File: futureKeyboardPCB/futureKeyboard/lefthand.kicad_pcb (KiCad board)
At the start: 2 copper layers, 168.9 x 88.3 mm, 126 parts, among them J1 Conn_01x01, J10 Conn_01x02, J11 Conn_01x01, J12 Conn_01x01, J13 Conn_01x04, J14 Conn_01x06, J15 Conn_01x06, J16 Conn_01x01, J17 Conn_01x15, J18 Conn_01x15, J19 Conn_01x15, J2 Conn_01x02, J20 Conn_01x15, J21 Conn_01x04, J22 Conn_01x04, J23 Conn_01x04, J24 Conn_01x04, J25 Conn_01x02, J26 Conn_01x01, J27 Conn_01x01, J28 Conn_01x01, J29 Conn_01x01, J3 Conn_01x01, J30 Conn_01x01, J31 Conn_01x01, J32 Conn_01x01, J33 Conn_01x01, J4 Conn_01x01, J5 Conn_01x04, J6 Conn_01x06, J7 Conn_01x06, J8 Conn_01x01, J9 Conn_01x01, P1 CONN_01X02, P2 CONN_01X06, P3 CONN_01X02, P4 CONN_01X06, Q1 2SC1815, Q2 2SC1815, Q3 2SC1815, Q4 2SC1815, Q5 2SC1815, Q6 2SC1815, SW1 SW_SPDT, SW10 SW_Push, SW11 SW_Push, SW12 SW_Push, SW13 SW_Push, SW14 SW_Push, SW15 SW_Push, SW16 SW_Push, SW17 SW_Push, SW18 SW_Push, SW19 SW_Push, SW2 SW_Push, SW20 SW_Push, SW21 SW_Push, SW22 SW_Push, SW23 SW_Push, SW24 SW_Push, SW25 SW_Push, SW3 SW_Push, SW4 SW_Push, SW5 SW_Push, SW6 SW_Push, SW7 SW_Push, SW8 SW_Push, SW9 SW_SPDT, U1 AMS1117-1.5, U2 ESP32, U3 AMS1117-1.5, U4 ESP32, U5 joystick

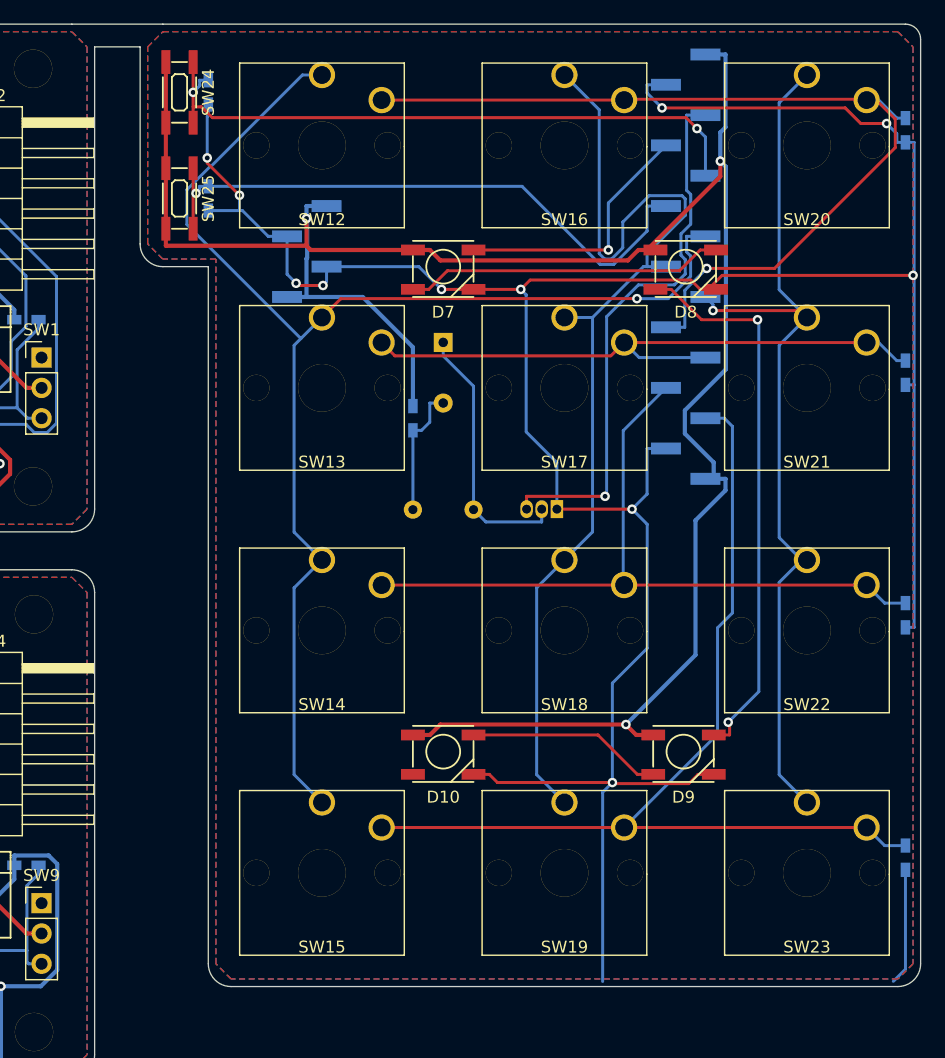
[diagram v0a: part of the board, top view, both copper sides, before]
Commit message: add arduino project using esp-now, new PCB
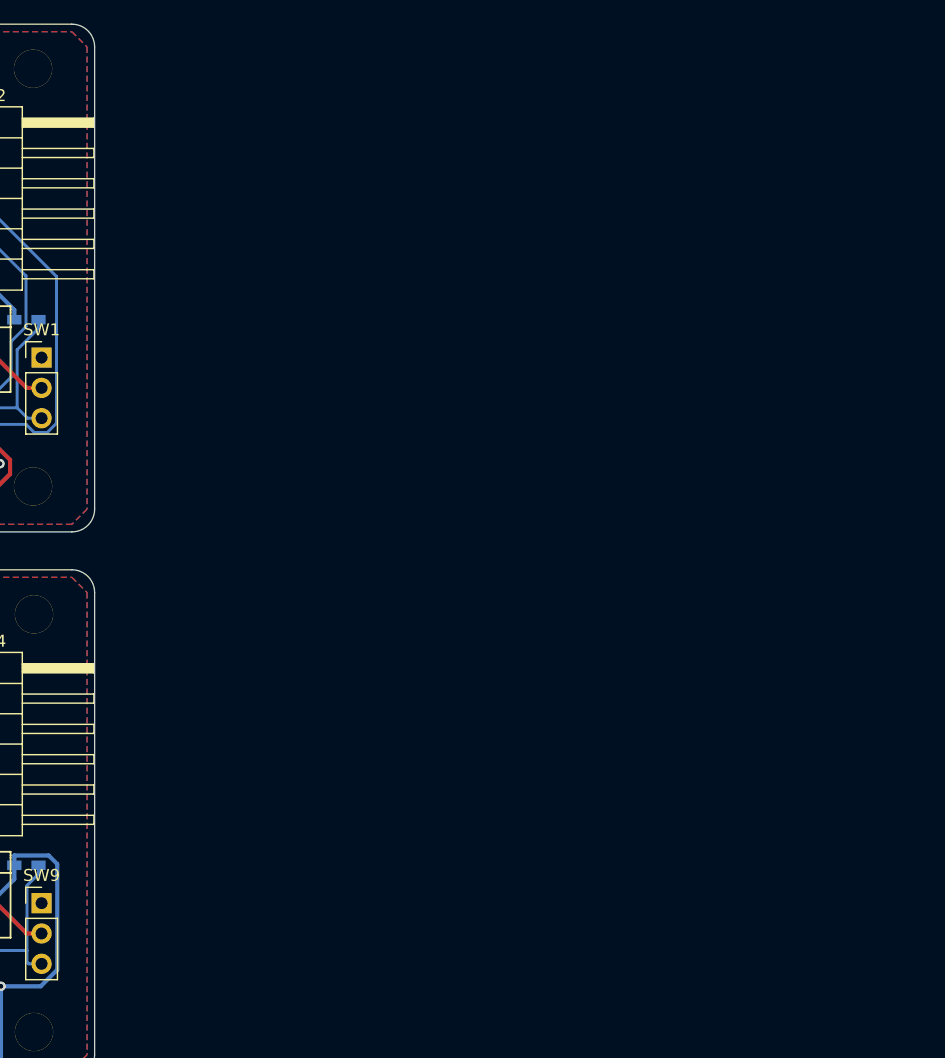
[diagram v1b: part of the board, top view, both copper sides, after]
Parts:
- removed D10, D7, D8, D9: WS2812B, akizukit:WS2812B
- removed D6: DIODE, Diode_THT:D_DO-35_SOD27_P5.08mm_Vertical_KathodeUp
- removed J20: Conn_01x15, Connector_PinHeader_2.54mm:PinHeader_1x15_P2.54mm_Vertical_SMD_Pin1Left
- removed J24: Conn_01x04, Connector_PinHeader_2.54mm:PinHeader_1x04_P2.54mm_Vertical_SMD_Pin1Left
- removed LS2: Speaker, akizukit:small_speaker
- removed Q6: 2SC1815, Package_TO_SOT_THT:TO-92_Inline
- removed R18, R20, R21, R22, R23, R24, R25: 1k, akizukit:SMD-1608
- removed SW12, SW13, SW14, SW15, SW16, SW17, SW18, SW19, SW20, SW21, SW22, SW23: SW_Push, akizukit:keySwitch
- removed SW24, SW25: SW_Push, akizukit:SMD_SW
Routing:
- net /Sheet5F548F88/GND2: track 251.9 -> 0.00 mm, vias 11 -> 0
- net /Sheet5F548F88/3v32: track 182.8 -> 0.00 mm, vias 3 -> 0
- net /Sheet5F548F88/c12: track 113.6 -> 0.00 mm, vias 1 -> 0
- net /Sheet5F548F88/c22: track 88.0 -> 0.00 mm
- net /Sheet5F548F88/r24: track 84.4 -> 0.00 mm
- net /Sheet5F548F88/r21: track 77.3 -> 0.00 mm, vias 1 -> 0
- net /Sheet5F548F88/c23: track 76.3 -> 0.00 mm, vias 1 -> 0
- net /Sheet5F548F88/r23: track 62.6 -> 0.00 mm
- net /Sheet5F548F88/button21: track 54.3 -> 0.00 mm, vias 2 -> 0
- net /Sheet5F548F88/r22: track 52.8 -> 0.00 mm
- net /Sheet5F548F88/button22: track 51.1 -> 0.00 mm, vias 1 -> 0
- net Net-(D8-Pad2): track 46.9 -> 0.00 mm, vias 2 -> 0
- net /Sheet5F548F88/spk2: track 46.4 -> 0.00 mm, vias 1 -> 0
- net Net-(D7-Pad2): track 26.8 -> 0.00 mm
- net Net-(D6-Pad1): track 22.3 -> 0.00 mm
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- removed copper zone on B.Cu, net /Sheet5F548F88/GND2
- removed copper zone on F.Cu, net /Sheet5F548F88/GND2
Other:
- board size 168.9 x 88.3 mm -> 99.7 x 88.3 mm
